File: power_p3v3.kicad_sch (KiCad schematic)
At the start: 24 parts, among them J1 LSHM-140-04.0-L-DV-A-N-K-TR, U1 LT8627SP

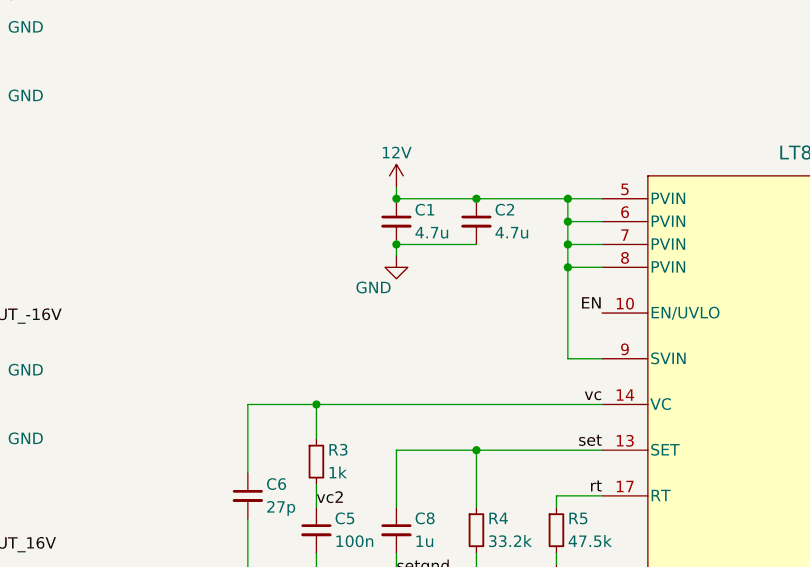
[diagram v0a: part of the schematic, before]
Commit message: Add Ferrite Beads
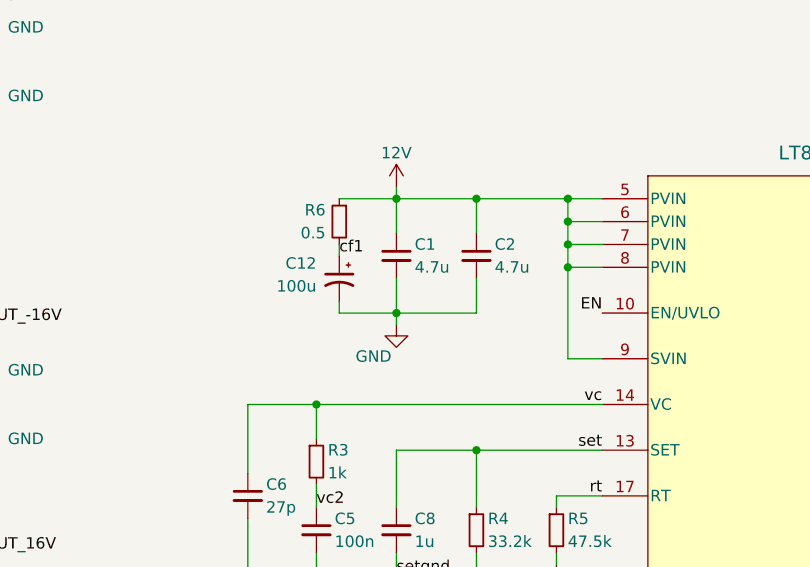
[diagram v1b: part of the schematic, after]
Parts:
- added C12: 100u, lib:T521X, symbol Device:C_Polarized_Small_US
- added R6: 0.5, Resistor_SMD:R_0603_1608Metric, symbol Device:R_Small
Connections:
- net 12V: now also R6.1
- net GND: now also C12.2
- new net cf1: C12.1, R6.2
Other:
- moved on the sheet: C1, C2

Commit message: update set resistor to thin film
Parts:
- R4: M Vishay -> Panasonic; MPN CRCW060333K2FKEA -> ERA-3AEB333V
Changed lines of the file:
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@@
 			)
 		)
-		(property "Description" "33.2 kOhms ±1% 0.125W, 1/8W Chip Resistor 0603 (1608 Metric) Automotive AEC-Q200 Thick Film"
+		(property "Description" "33 kOhms ±0.1% 0.1W, 1/10W Chip Resistor 0603 (1608 Metric) Automotive AEC-Q200 Thin Film"
 			(at 105.41 97.79 0)
 			(effects
@@
 			)
 		)
-		(property "M" "Vishay"
+		(property "M" "Panasonic"
 			(at 105.41 97.79 0)
 			(effects
@@
 			)
 		)
-		(property "MPN" "CRCW060333K2FKEA"
+		(property "MPN" "ERA-3AEB333V"
 			(at 105.41 97.79 0)
 			(effects

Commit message: Update
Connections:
- net GND: no longer J1.62 (Pin_62), J1.64 (Pin_64), J1.66 (Pin_66), J1.68 (Pin_68), J1.70 (Pin_70)
- new net VOUT_16V: J1.62 (Pin_62), J1.64 (Pin_64), J1.66 (Pin_66), J1.68 (Pin_68), J1.70 (Pin_70)
